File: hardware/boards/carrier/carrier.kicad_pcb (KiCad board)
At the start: 4 copper layers, 106 x 34.3 mm, 70 parts, among them J1 XT30PW(2+2), Q1 IPB020N10N5LF, Q2 2N7002, Q3 2N7002, SW1 SKSCLCE010, U1 STM32C092GCU7, U2 LM5163DDAR, U3 LMX5069MS, U4 INA237AIDGSR, U5 TCAN3413DR

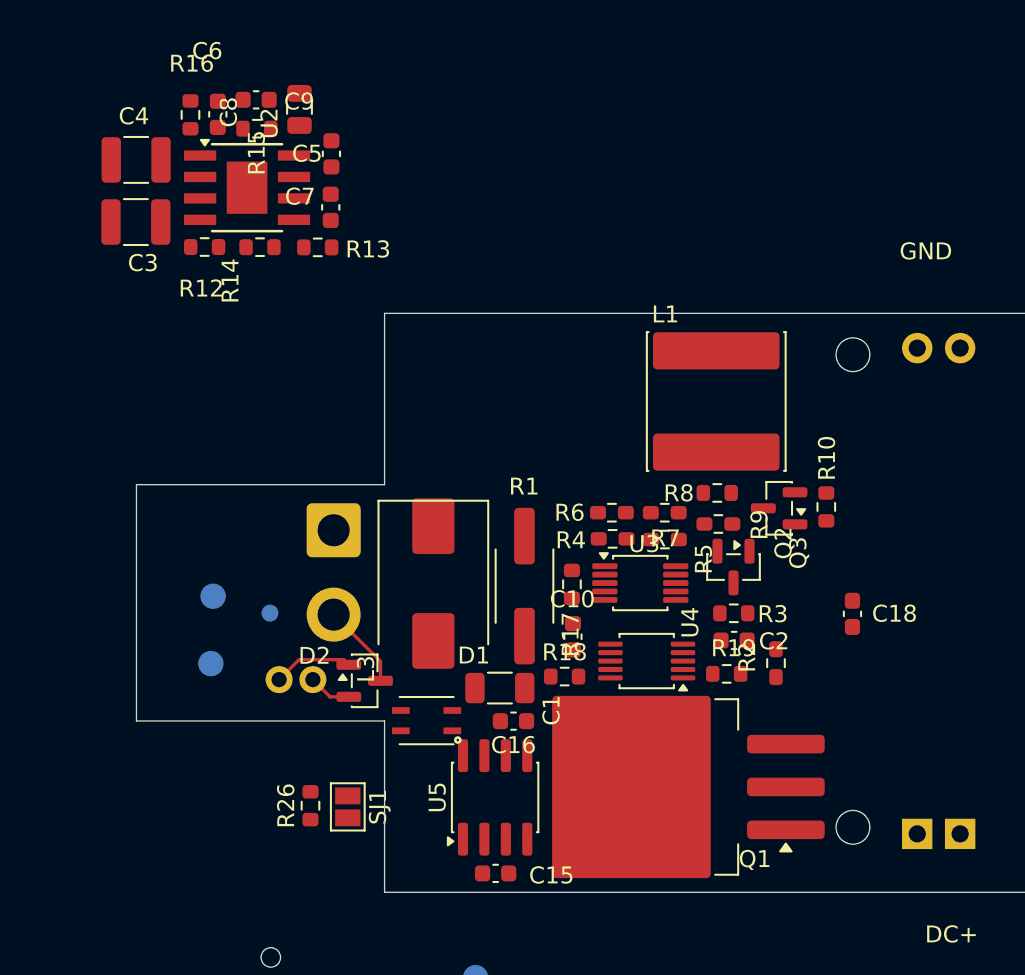
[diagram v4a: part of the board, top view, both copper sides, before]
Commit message: Rebuild carrier left-side component placement
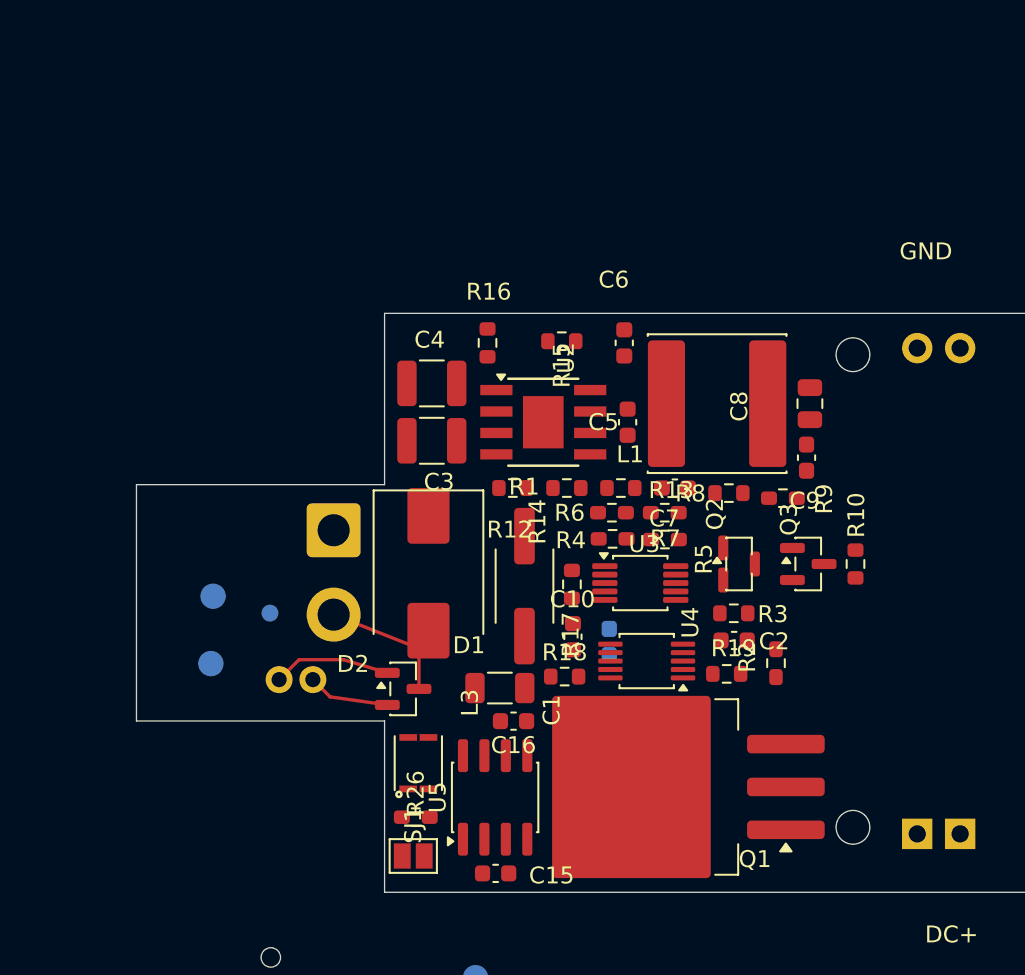
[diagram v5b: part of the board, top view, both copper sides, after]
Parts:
- C18: moved to B.Cu
- moved C9 38.9 mm to (140.5, 104.9), turned to -90 degrees
- moved C8 34.9 mm to (140.7, 101.7)
- moved C6 27.6 mm to (129.7, 98.1)
- moved C7 26.3 mm to (132.7, 106.7), turned to 0 degrees
- moved C5 23.7 mm to (129.9, 102.8)
- moved R12 23.2 mm to (123.1, 106.7)
- moved R14 23.1 mm to (126.3, 106.7)
- moved R13 22.9 mm to (129.5, 106.7)
- moved U2 22.4 mm to (124.9, 102.8)
- moved R16 22.2 mm to (121.6, 98.1)
- moved R15 22.0 mm to (126.0, 98.0)
- moved C4 22.0 mm to (118.3, 100.5)
- moved C3 21.8 mm to (118.3, 103.9)
- moved C18 14.5 mm to (128.8, 115.8)
- moved R26 6.28 mm to (117.3, 126.2), turned to 0 degrees
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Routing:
- net GND: track 5.07 -> 7.84 mm
- net /CAN_BUS_N: track 2.55 -> 4.87 mm
- net /CAN_BUS_P: track 4.74 -> 7.01 mm

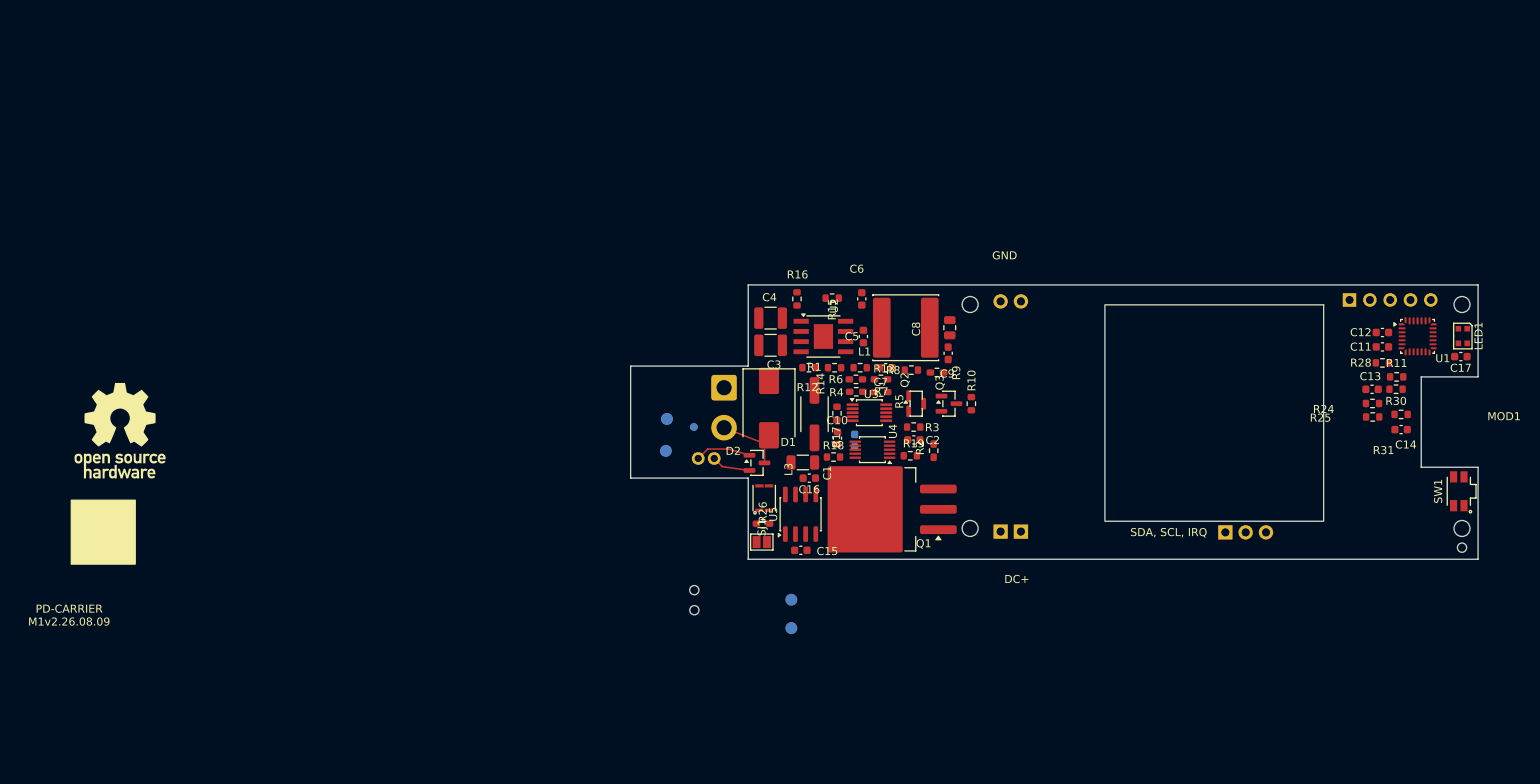
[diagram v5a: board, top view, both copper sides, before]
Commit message: Stage carrier circuit constellations off-board
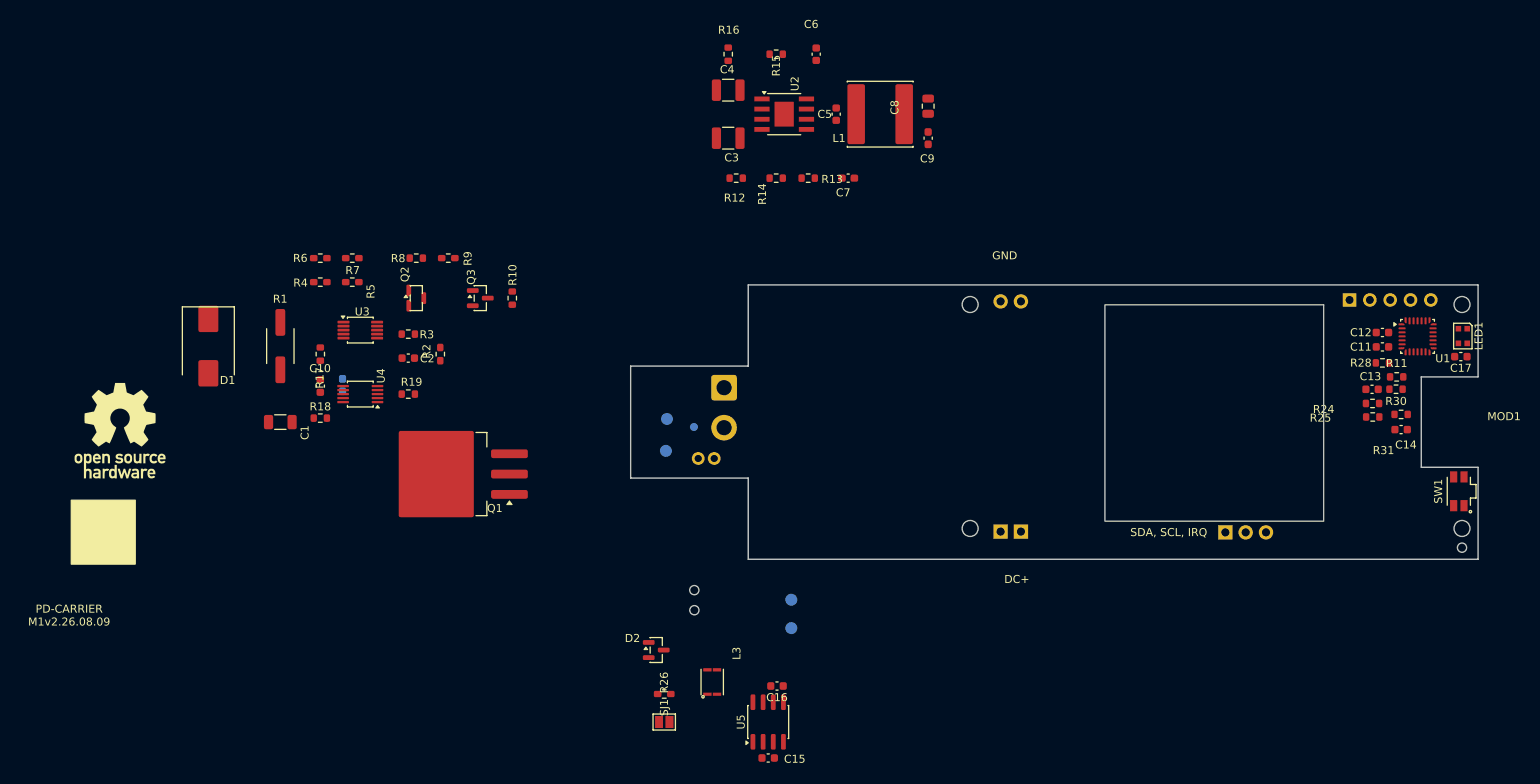
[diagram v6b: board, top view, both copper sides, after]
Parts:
- moved D1 70.5 mm to (48.0, 104.0)
- moved R6 68.7 mm to (62.0, 93.0)
- moved R4 68.4 mm to (62.0, 96.0)
- moved R7 67.8 mm to (66.0, 93.0)
- moved R5 67.5 mm to (66.0, 96.0)
- moved R1 67.3 mm to (57.0, 104.0)
- moved C1 65.5 mm to (57.0, 113.5)
- moved R17 65.0 mm to (62.0, 105.0)
- moved C10 65.0 mm to (62.0, 109.0)
- moved U3 64.5 mm to (67.0, 102.0)
- moved C18 64.4 mm to (64.8, 108.9)
- moved U4 64.4 mm to (67.0, 110.0)
- moved R18 64.4 mm to (62.0, 113.0)
- moved R3 64.2 mm to (73.0, 102.5)
- moved C2 64.0 mm to (73.0, 105.5)
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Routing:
- net GND: track 7.84 -> 0.00 mm
- net /CAN_BUS_P: track 7.01 -> 0.00 mm
- net /CAN_BUS_N: track 4.87 -> 0.00 mm

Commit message: Capture off-board constellation edits
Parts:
- C18: moved to F.Cu
- moved D1 70.8 mm to (118.3, 111.8)
- moved R1 67.1 mm to (123.7, 111.5)
- moved Q1 55.8 mm to (133.8, 119.9), turned to 90 degrees
- moved D2 25.9 mm to (114.3, 118.2)
- moved C18 2.98 mm to (65.1, 105.9)

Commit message: Separate carrier U3 and U4 constellations
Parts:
- moved R18 25.3 mm to (37.5, 106.7)
- moved R17 24.6 mm to (37.5, 103.4)
- moved C18 24.2 mm to (41.0, 103.4)
- moved R19 22.6 mm to (51.0, 105.0)
- moved U4 22.6 mm to (45.0, 105.0)
- moved C10 21.1 mm to (41.0, 106.7)
- moved C1 7.81 mm to (62.0, 107.5)
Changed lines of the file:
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@@
 	(footprint "Resistor_SMD:R_0603_1608Metric"
 		(layer "F.Cu")
-		(at 62 113)
+		(at 37.5 106.7)
 		(descr "Resistor SMD 0603 (1608 Metric), square (rectangular) end terminal, IPC-7351 nominal, (Body size source: IPC-SM-782 page 72, https://www.pcb-3d.com/wordpress/wp-content/uploads/ipc-sm-782a_amendment_1_and_2.pdf)")
 		(tags "resistor")
@@
 	(footprint "Resistor_SMD:R_0603_1608Metric"
 		(layer "F.Cu")
-		(at 62 105 90)
+		(at 37.5 103.4 90)
 		(descr "Resistor SMD 0603 (1608 Metric), square (rectangular) end terminal, IPC-7351 nominal, (Body size source: IPC-SM-782 page 72, https://www.pcb-3d.com/wordpress/wp-content/uploads/ipc-sm-782a_amendment_1_and_2.pdf)")
 		(tags "resistor")
@@
 	(footprint "Capacitor_SMD:C_1206_3216Metric"
 		(layer "F.Cu")
-		(at 57 113.5 180)
+		(at 62 107.5 180)
 		(descr "Capacitor SMD 1206 (3216 Metric), square (rectangular) end terminal, IPC-7351 nominal, (Body size source: IPC-SM-782 page 76, https://www.pcb-3d.com/wordpress/wp-content/uploads/ipc-sm-782a_amendment_1_and_2.pdf)")
 		(tags "capacitor")
@@
 	(footprint "Capacitor_SMD:C_0603_1608Metric"
 		(layer "F.Cu")
-		(at 62 109 -90)
+		(at 41 106.7 -90)
 		(descr "Capacitor SMD 0603 (1608 Metric), square (rectangular) end terminal, IPC-7351 nominal, (Body size source: IPC-SM-782 page 76, https://www.pcb-3d.com/wordpress/wp-content/uploads/ipc-sm-782a_amendment_1_and_2.pdf)")
 		(tags "capacitor")
@@
 	(footprint "Package_SO:TSSOP-10_3x3mm_P0.5mm"
 		(layer "F.Cu")
-		(at 67 110 180)
+		(at 45 105 180)
 		(descr "TSSOP, 10 Pin (https://www.ti.com/lit/ml/mpds035c/mpds035c.pdf, https://www.ti.com/lit/ds/symlink/ads1115.pdf#page=50, https://www.nxp.com/docs/en/package-information/SOT552-1.pdf)")
 		(tags "TSSOP SO Texas_DGS0010A Texas_VSSOP-10 NXP_SOT552-1 MSOP-10_3x3mm_P0.5mm VSSOP-10_3x3mm_P0.5mm")
@@
 	(footprint "Resistor_SMD:R_0603_1608Metric"
 		(layer "F.Cu")
-		(at 73 110 180)
+		(at 51 105 180)
 		(descr "Resistor SMD 0603 (1608 Metric), square (rectangular) end terminal, IPC-7351 nominal, (Body size source: IPC-SM-782 page 72, https://www.pcb-3d.com/wordpress/wp-content/uploads/ipc-sm-782a_amendment_1_and_2.pdf)")
 		(tags "resistor")
@@
 	(footprint "Capacitor_SMD:C_0603_1608Metric"
 		(layer "F.Cu")
-		(at 65.08 105.905 -90)
+		(at 41 103.4 -90)
 		(descr "Capacitor SMD 0603 (1608 Metric), square (rectangular) end terminal, IPC-7351 nominal, (Body size source: IPC-SM-782 page 76, https://www.pcb-3d.com/wordpress/wp-content/uploads/ipc-sm-782a_amendment_1_and_2.pdf)")
 		(tags "capacitor")
